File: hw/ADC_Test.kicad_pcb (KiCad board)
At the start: 2 copper layers, 57 x 32 mm, 74 parts, among them J1 SMA SENSOR IN, J2 9V IN, J3 PMOD (ZedBoard), J4 SMA MON, U1 OPA2365, U2 OPA2365, U3 THS4531, U4 ADS7057, U5 XC6206P332MR-G, U6 LM393, U7 AMS1117-5.0

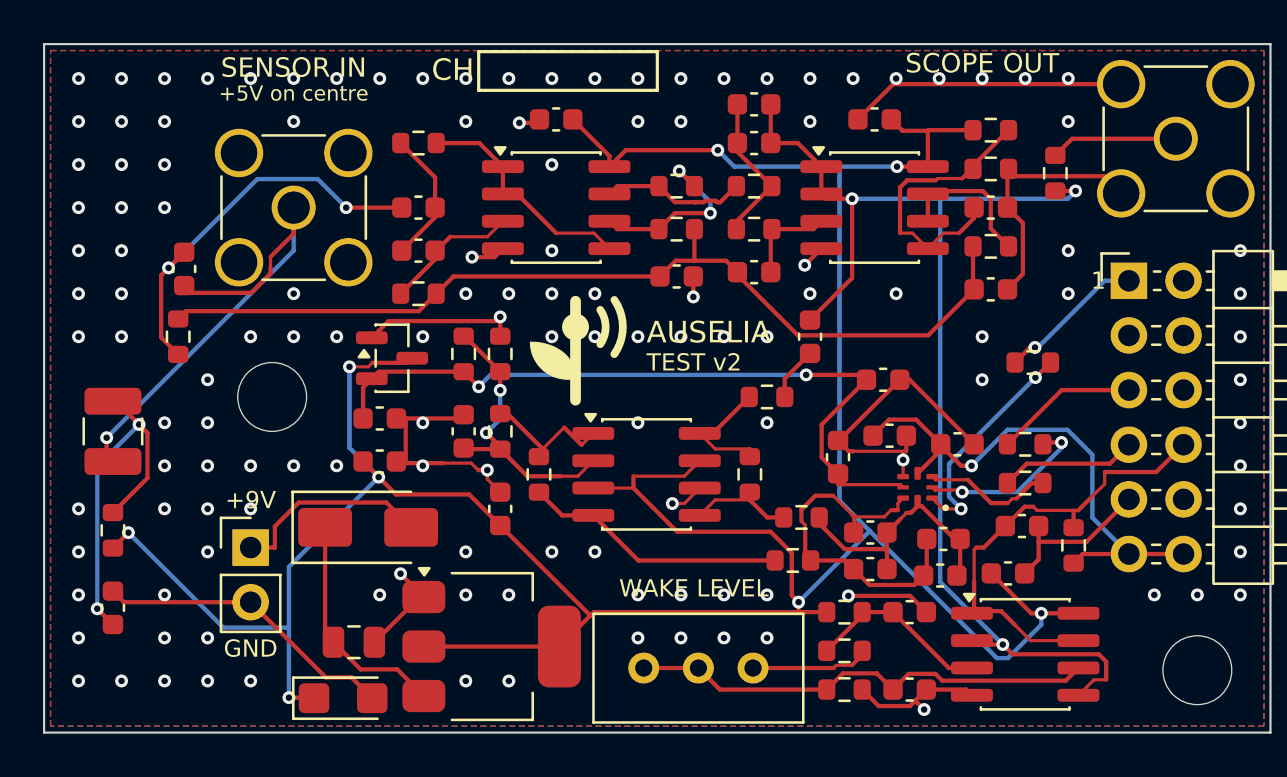
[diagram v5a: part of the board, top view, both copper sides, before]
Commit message: Solder jumper JP1 in the head power feed (cut it to use a generator on SENSOR IN); re-routed, files and manual regenerated
Co-Authored-By: Claude Sonnet 5.5 <noreply@anthropic.com>
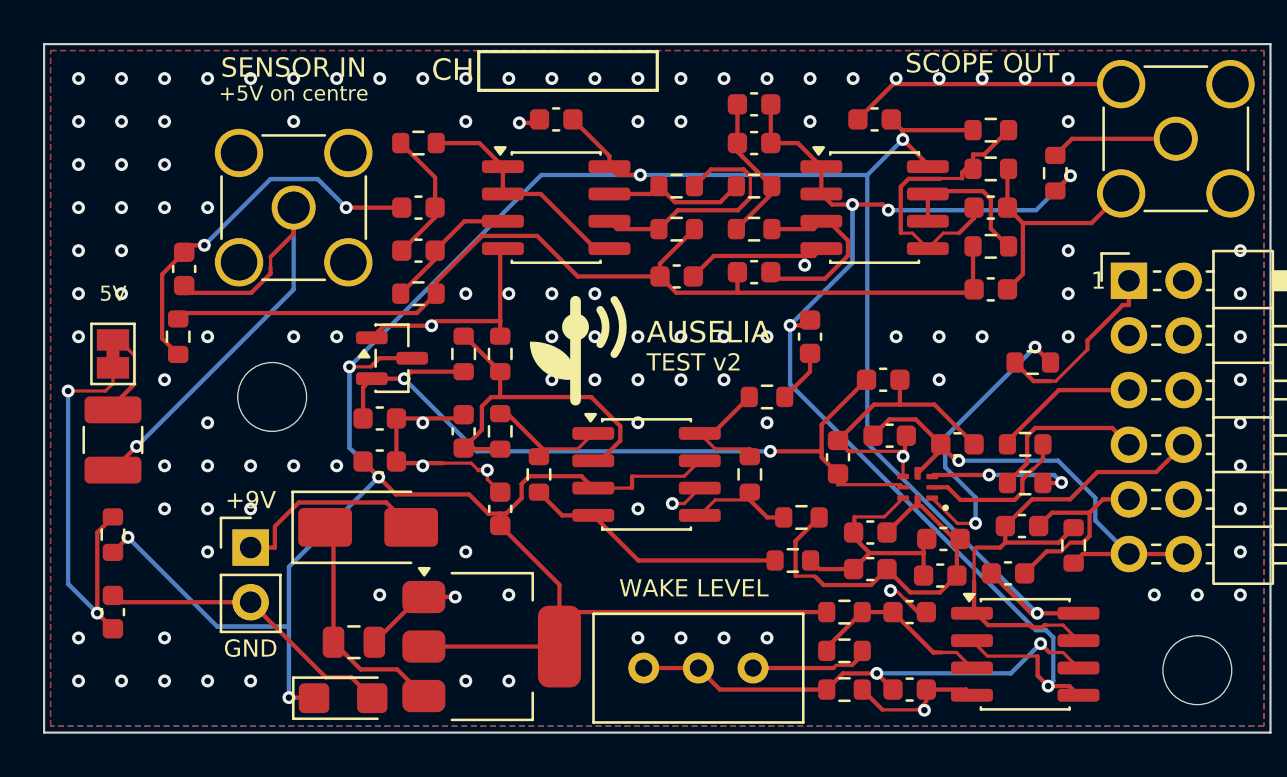
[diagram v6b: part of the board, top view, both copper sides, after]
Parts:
- added JP1: HEAD PWR, Jumper:SolderJumper-2_P1.3mm_Bridged_Pad1.0x1.5mm, F.Cu at (103.2, 114.4)
- moved L2 0.40 mm to (103.2, 118.4)
- moved C32 0.20 mm to (103.2, 126.4)
- moved R26 0.20 mm to (103.2, 122.8)
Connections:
- L2 pad 2: HEAD_PWR -> HEAD_PWR_L
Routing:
- net GND: track 99.8 -> 106.1 mm, vias 134 -> 122
- net AINM: track 12.2 -> 18.5 mm
- net AINP: track 16.9 -> 12.1 mm
- net LP_B: track 4.47 -> 8.92 mm
- net HEAD_PWR_L: track 0.00 -> 4.24 mm
- net VOCM: track 13.4 -> 17.1 mm, vias 2 -> 0
- net CS_A: track 10.5 -> 14.0 mm
- net WAKE_N: track 21.4 -> 24.2 mm
- net GN_FB: track 8.70 -> 11.4 mm, vias 2 -> 0
- net HEAD_PWR: track 17.0 -> 19.6 mm
- net +3V3: track 24.9 -> 22.4 mm
- net VMID5: track 44.0 -> 45.9 mm
- net CS: track 6.87 -> 8.49 mm, vias 1 -> 0
- net AVDD: track 34.9 -> 36.4 mm
- net SCLK: track 6.38 -> 7.77 mm
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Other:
- board text added: "5V"

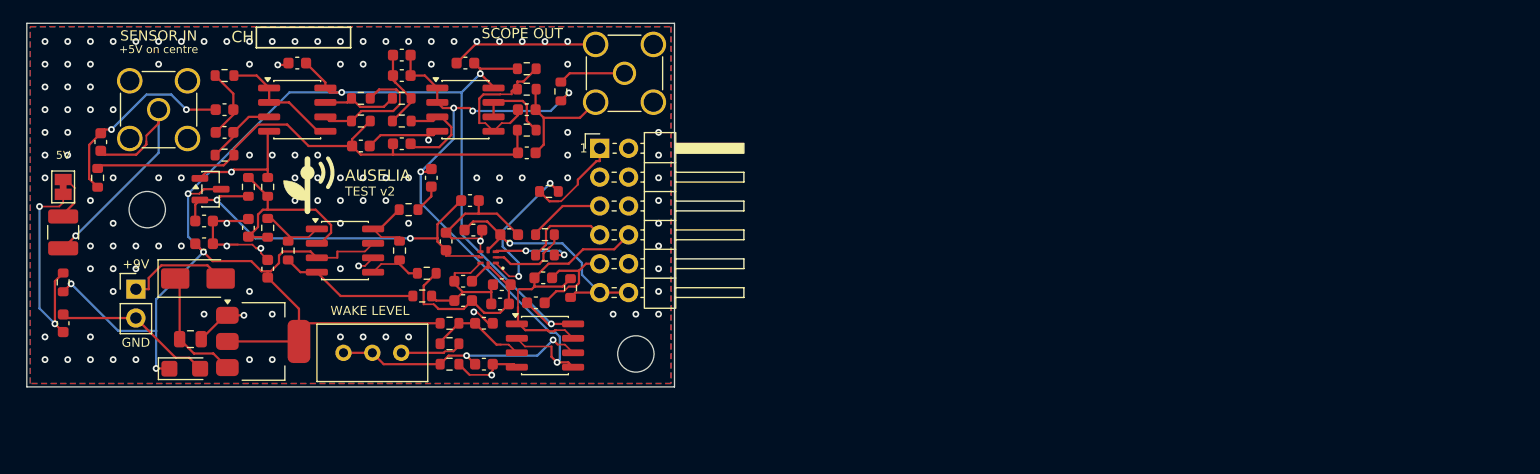
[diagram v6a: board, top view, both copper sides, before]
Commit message: 5 V input (USB-C and header, SS14 each, ferrite), 18 test points, no 9 V battery, AMS1117 and tantalum removed; chain re-simulated at the 4.6 V rail; manual and README updated
Co-Authored-By: Claude Sonnet 5.5 <noreply@anthropic.com>
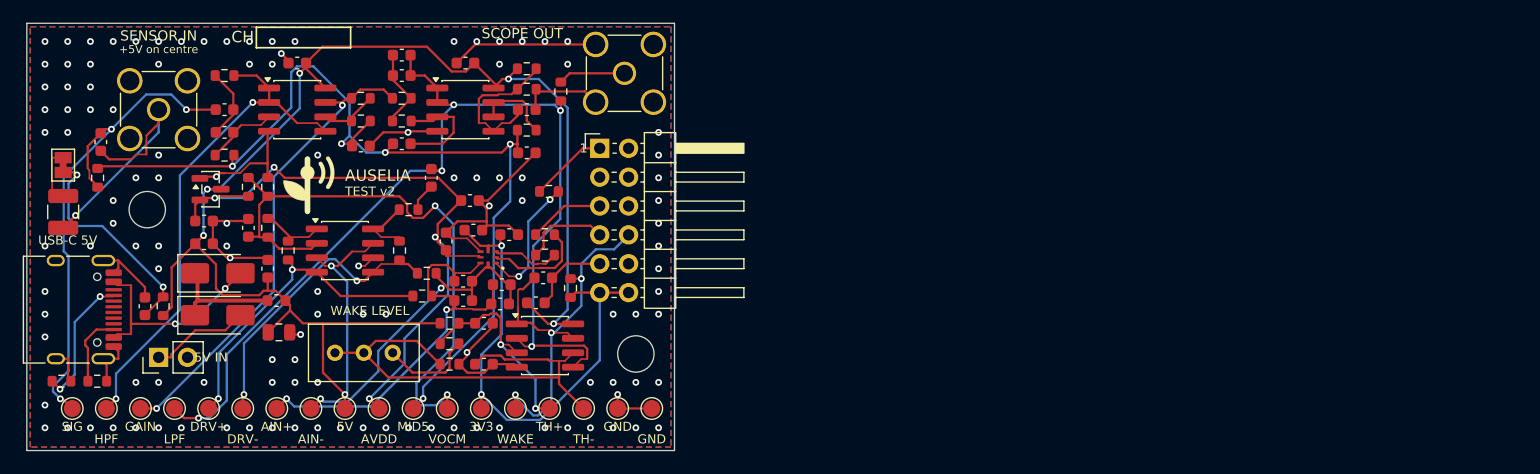
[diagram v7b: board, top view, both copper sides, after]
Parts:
- removed C29: 22uF 10V tantalum, Capacitor_Tantalum_SMD:CP_EIA-3216-18_Kemet-A
- removed U7: AMS1117-5.0, Package_TO_SOT_SMD:SOT-223-3_TabPin2
- added D2: SS14, Diode_SMD:D_SMA, F.Cu at (116.8, 125.7)
- added FB1: 120R 2A, Inductor_SMD:L_0603_1608Metric, F.Cu at (122.0, 124.4)
- added J7: 5V IN, Connector_PinHeader_2.54mm:PinHeader_1x02_P2.54mm_Vertical, F.Cu at (111.6, 129.4)
- added R32: 5.1k, Resistor_SMD:R_0603_1608Metric, F.Cu at (103.0, 131.5)
- added R33: 5.1k, Resistor_SMD:R_0603_1608Metric, F.Cu at (106.2, 131.5)
- added TP10: AINM, TestPoint:TestPoint_Pad_D1.5mm, F.Cu at (125.0, 133.9)
- added TP11: +5V, TestPoint:TestPoint_Pad_D1.5mm, F.Cu at (128.0, 133.9)
- added TP12: AVDD, TestPoint:TestPoint_Pad_D1.5mm, F.Cu at (131.0, 133.9)
- added TP13: VMID5, TestPoint:TestPoint_Pad_D1.5mm, F.Cu at (134.0, 133.9)
- added TP14: VOCM, TestPoint:TestPoint_Pad_D1.5mm, F.Cu at (137.0, 133.9)
- added TP15: +3V3, TestPoint:TestPoint_Pad_D1.5mm, F.Cu at (140.0, 133.9)
- added TP16: WAKE_N, TestPoint:TestPoint_Pad_D1.5mm, F.Cu at (143.0, 133.9)
- added TP17: VTH_H, TestPoint:TestPoint_Pad_D1.5mm, F.Cu at (146.0, 133.9)
- added TP18: VTH_L, TestPoint:TestPoint_Pad_D1.5mm, F.Cu at (149.0, 133.9)
- added TP19: GND, TestPoint:TestPoint_Pad_D1.5mm, F.Cu at (152.0, 133.9)
- added TP20: GND, TestPoint:TestPoint_Pad_D1.5mm, F.Cu at (155.0, 133.9)
- added TP3: SIG_IN, TestPoint:TestPoint_Pad_D1.5mm, F.Cu at (104.0, 133.9)
- added TP4: HPF_OUT, TestPoint:TestPoint_Pad_D1.5mm, F.Cu at (107.0, 133.9)
- added TP5: GAIN_OUT, TestPoint:TestPoint_Pad_D1.5mm, F.Cu at (110.0, 133.9)
- added TP6: LPF_OUT, TestPoint:TestPoint_Pad_D1.5mm, F.Cu at (113.0, 133.9)
- added TP7: DRV_OUTP, TestPoint:TestPoint_Pad_D1.5mm, F.Cu at (116.0, 133.9)
- added TP8: DRV_OUTN, TestPoint:TestPoint_Pad_D1.5mm, F.Cu at (119.0, 133.9)
- added TP9: AINP, TestPoint:TestPoint_Pad_D1.5mm, F.Cu at (122.0, 133.9)
- C23: value 10uF 25V -> 22uF 25V
- J2: value 9V IN -> USB-C 5V; footprint Connector_PinHeader_2.54mm:PinHeader_1x02_P2.54mm_Vertical -> Connector_USB:USB_C_Receptacle_HRO_TYPE-C-31-M-12
- moved R26 9.05 mm to (112.0, 124.9)
- moved C23 7.81 mm to (122.2, 127.2)
- moved C32 7.35 mm to (110.4, 124.9)
- moved J2 6.26 mm to (103.6, 125.2), turned to -90 degrees
- moved JP1 1.92 mm to (103.2, 112.5)
- moved L2 1.80 mm to (103.2, 116.6)
- moved D1 1.80 mm to (116.8, 122.0)
- moved RV1 0.75 mm to (132.2, 129.0)
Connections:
- C23 pad 1: +9VP -> +5V
- D1 pad 1: +9VP -> +5V_IN
- D1 pad 2: +9V_IN -> VBUS
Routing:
- net VMID5: track 45.9 -> 83.3 mm, vias 0 -> 5
- net VOCM: track 17.1 -> 53.0 mm, vias 0 -> 2
- net LPF_OUT: track 56.0 -> 91.3 mm
- net GAIN_OUT: track 6.67 -> 41.8 mm, vias 0 -> 2
- net HPF_OUT: track 10.8 -> 44.5 mm, vias 0 -> 2
- net SIG_IN: track 17.6 -> 45.5 mm, vias 2 -> 3
- net AINP: track 12.1 -> 37.7 mm, vias 0 -> 2
- net +3V3: track 22.4 -> 45.0 mm, vias 1 -> 2
- net AVDD: track 36.4 -> 58.5 mm, vias 2 -> 4
- net DRV_OUTN: track 4.90 -> 26.2 mm, vias 0 -> 2
- net VTH_L: track 23.0 -> 43.1 mm, vias 2 -> 0
- net VBUS: track 0.00 -> 19.1 mm, vias 0 -> 2
- net DRV_OUTP: track 12.3 -> 27.8 mm, vias 0 -> 2
- net USB_CC1: track 0.00 -> 11.8 mm, vias 0 -> 2
- net WAKE_N: track 24.2 -> 35.8 mm, vias 0 -> 3
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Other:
- board size 57 x 32 mm -> 57 x 37.6 mm
- board text added: "3V3"
- board text added: "5V IN"
- board text added: "AIN+"
- board text added: "AIN-"
- board text added: "AVDD"
- board text added: "DRV+"
- board text added: "DRV-"
- board text added: "GAIN"
- board text added: "HPF"
- board text added: "LPF"
- board text added: "MID5"
- board text added: "SIG"
- board text added: "TH+"
- board text added: "TH-"
- board text added: "USB-C 5V"
- board text added: "VOCM"
- board text added: "WAKE"
- board text removed: "+9V"

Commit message: v3 low-power 3.3 V board: 125 x 21.5 mm narrow layout, PMOD-powered, listener (WAKE_N/BIG_N), routed to 0 unconnected
Manual and README still describe the v2 (5 V, USB-C) board and need regeneration.

Co-Authored-By: Claude Sonnet 5.5 <noreply@anthropic.com>
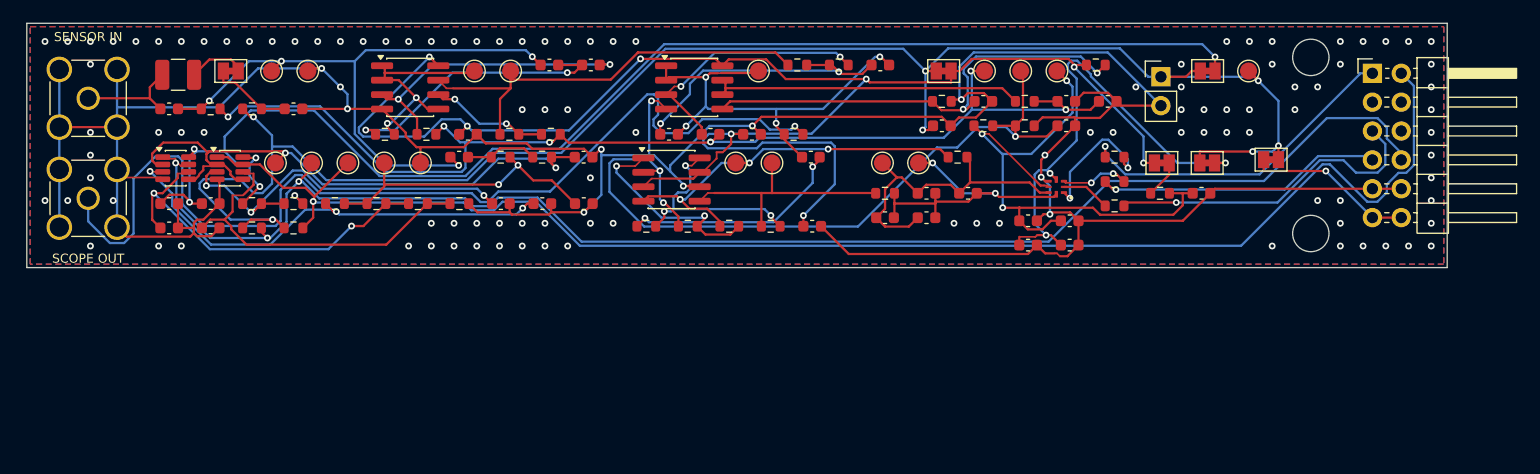
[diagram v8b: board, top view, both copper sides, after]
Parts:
- removed C30: 1uF, Capacitor_SMD:C_0603_1608Metric
- removed C31: DNP, Capacitor_SMD:C_0603_1608Metric
- removed D1, D2: SS14, Diode_SMD:D_SMA
- removed FB1: 120R 2A, Inductor_SMD:L_0603_1608Metric
- removed J2: USB-C 5V, Connector_USB:USB_C_Receptacle_HRO_TYPE-C-31-M-12
- removed R32, R33: 5.1k, Resistor_SMD:R_0603_1608Metric
- removed RV1: 20k trim, Potentiometer_THT:Potentiometer_Bourns_3296W_Vertical
- removed U5: XC6206P332MR-G, Package_TO_SOT_SMD:SOT-23
- added C40: 100pF C0G, Capacitor_SMD:C_0603_1608Metric, F.Cu at (138.1, 111.8)
- added C41: 100pF C0G, Capacitor_SMD:C_0603_1608Metric, F.Cu at (149.0, 111.8)
- added C42: 1uF, Capacitor_SMD:C_0603_1608Metric, F.Cu at (149.0, 115.9)
- added C43: 100nF, Capacitor_SMD:C_0603_1608Metric, F.Cu at (141.7, 115.9)
- added C44: 100nF, Capacitor_SMD:C_0603_1608Metric, F.Cu at (116.2, 118.0)
- added C45: 100nF, Capacitor_SMD:C_0603_1608Metric, F.Cu at (116.2, 115.9)
- added JP2: LISTENER LINK, Jumper:SolderJumper-2_P1.3mm_Bridged_Pad1.0x1.5mm, F.Cu at (203.9, 104.2)
- added JP3: CAPTURE LINK, Jumper:SolderJumper-2_P1.3mm_Bridged_Pad1.0x1.5mm, F.Cu at (180.7, 104.2)
- added JP4: AVDD LINK, Jumper:SolderJumper-2_P1.3mm_Bridged_Pad1.0x1.5mm, F.Cu at (199.9, 112.3)
- added JP5: DVDD LINK, Jumper:SolderJumper-2_P1.3mm_Bridged_Pad1.0x1.5mm, F.Cu at (203.9, 112.3)
- added JP6: PMOD 3V3, Jumper:SolderJumper-2_P1.3mm_Bridged_Pad1.0x1.5mm, F.Cu at (209.5, 112.0)
- added R34: 10R, Resistor_SMD:R_0603_1608Metric, F.Cu at (199.7, 115.0)
- added R35: 10k, Resistor_SMD:R_0603_1608Metric, F.Cu at (141.7, 111.8)
- added R36: 2.2k, Resistor_SMD:R_0603_1608Metric, F.Cu at (145.3, 111.8)
- added R39: 18k, Resistor_SMD:R_0603_1608Metric, F.Cu at (127.1, 115.9)
- added R40: 18k, Resistor_SMD:R_0603_1608Metric, F.Cu at (130.8, 115.9)
- added R41: 33k, Resistor_SMD:R_0603_1608Metric, F.Cu at (134.4, 115.9)
- added R42: 47k, Resistor_SMD:R_0603_1608Metric, F.Cu at (123.5, 118.0)
- added U9: TLV7022, Package_TO_SOT_SMD:SOT-23-8, F.Cu at (117.9, 112.8)
- C21: value 1uF -> 10uF
- C23: value 22uF 25V -> 10uF; footprint Capacitor_SMD:C_0805_2012Metric -> Capacitor_SMD:C_0603_1608Metric
- J7: value 5V IN -> 3V3 IN
- R21, R23: value 33k -> 1M
- R22: value 1.00k -> 33k
- R24: value 10k -> 47k
- TP11: value +5V -> +3V3
- TP15: value +3V3 -> LST
- TP17: value VTH_H -> BIG_N
- TP18: value VTH_L -> REFL
- U6: value LM393 -> TLV7022; footprint Package_SO:SOIC-8_3.9x4.9mm_P1.27mm -> Package_TO_SOT_SMD:SOT-23-8
- moved H1 103.3 mm to (213.0, 103.0)
- moved J7 91.6 mm to (199.8, 104.7), turned to 0 degrees
- moved C21 87.8 mm to (203.4, 115.0)
- moved TP11 84.9 mm to (207.5, 104.2)
- moved C13 72.5 mm to (191.5, 109.0), turned to 0 degrees
- moved J3 68.3 mm to (218.4, 104.4)
- moved R15 66.8 mm to (187.8, 109.0), turned to 0 degrees
- moved TP12 66.6 mm to (190.7, 104.2)
- moved C9 65.8 mm to (195.1, 106.9)
- moved R14 64.9 mm to (184.2, 109.0), turned to 0 degrees
- moved C23 61.1 mm to (180.5, 109.0)
- moved H2 60.3 mm to (213.0, 118.5)
- moved TP6 59.4 mm to (164.4, 104.2)
- moved TP14 58.6 mm to (187.5, 104.2)
- moved TP13 58.4 mm to (184.3, 104.2)
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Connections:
- C10 pad 1: +5V -> +3V3_C
- C12 pad 1: +5V -> +3V3_C
- C19 pad 1: +3V3 -> DVDD
- C20 pad 1: +3V3 -> DVDD
- C23 pad 1: +5V -> +3V3
- C26 pad 1: VTH_H -> TH1P
- C27 pad 1: VTH_L -> TH1M
- C28 pad 1: +5V -> +3V3_L
- C3 pad 1: +5V -> +3V3_C
- J3 pad 11: +3V3 -> +3V3_PMOD
- J3 pad 12: +3V3 -> +3V3_PMOD
- J3 pad 2: unconnected-(J3-Pin_2-Pad2) -> BIG_N
- J7 pad 1: +5V_EXT -> +3V3
- R21 pad 1: +5V -> +3V3_L
- R21 pad 2: VTH_H -> TH2P
- R22 pad 1: VTH_H -> TH2P
- R22 pad 2: PTOP -> TH1P
- R23 pad 1: VTH_L -> TH2M
- R26 pad 1: +5V -> +3V3
- R7 pad 1: +5V -> +3V3_C
- TP11 pad 1: +5V -> +3V3
- TP15 pad 1: +3V3 -> LST
- TP17 pad 1: VTH_H -> BIG_N
- TP18 pad 1: VTH_L -> REFL
- U1 pad 8: +5V -> +3V3_C
- U2 pad 8: +5V -> +3V3_C
- U3 pad 3: +5V -> +3V3_C
- U3 pad 7: +5V -> +3V3_C
- U4 pad 4: +3V3 -> DVDD
- U6 pad 2: LPF_OUT -> LST
- U6 pad 3: VTH_H -> TH1P
- U6 pad 5: LPF_OUT -> LST
- U6 pad 6: VTH_L -> TH1M
- U6 pad 8: +5V -> +3V3_L
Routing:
- net GND: track 109.5 -> 297.4 mm
- net +3V3_C: track 0.00 -> 143.0 mm, vias 0 -> 8
- net +5V: track 141.1 -> 0.00 mm, vias 7 -> 0
- net BIG_N: track 0.00 -> 131.1 mm, vias 0 -> 1
- net +3V3_L: track 0.00 -> 120.2 mm, vias 0 -> 5
- net +3V3: track 45.0 -> 151.1 mm, vias 2 -> 7
- net WAKE_N: track 35.8 -> 132.0 mm
- net MON: track 5.92 -> 89.6 mm, vias 0 -> 1
- net LST: track 0.00 -> 52.9 mm, vias 0 -> 2
- net LPF_OUT: track 91.3 -> 39.4 mm, vias 5 -> 4
- net TH1P: track 0.00 -> 43.9 mm, vias 0 -> 4
- net VTH_L: track 43.1 -> 0.00 mm
- net DVDD: track 0.00 -> 42.5 mm, vias 0 -> 3
- net TH2P: track 0.00 -> 34.0 mm, vias 0 -> 3
- net TH1M: track 0.00 -> 33.6 mm, vias 0 -> 2
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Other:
- board size 57 x 37.6 mm -> 125 x 21.5 mm
- board text added: "1 CS 7 BIG_N"
- board text added: "4 SCK 10 WAKE_N"
- board text added: "ADS7057 test board v3"
- board text added: "BIG"
- board text added: "CAPTURE"
- board text added: "DVDD"
- board text added: "HEAD"
- board text added: "LISTEN"
- board text added: "LST"
- board text added: "PMOD (J3)"
- board text added: "PMOD 3V3"
- board text added: "REFL"
- board text removed: "+5V on centre"
- board text removed: "1"
- board text removed: "1 CS 7 -"
- board text removed: "4 SCK 10 nWAKE"
- board text removed: "5V"
- board text removed: "5V IN"
- board text removed: "ADS7057 test board v2"
- board text removed: "AUSELIA"
- board text removed: "CH"
- board text removed: "TEST v2"
- board text removed: "TH+"
- board text removed: "TH-"
- board text removed: "USB-C 5V"
- board text removed: "WAKE LEVEL"
- board text removed: "ZedBoard PMOD (J3)"
